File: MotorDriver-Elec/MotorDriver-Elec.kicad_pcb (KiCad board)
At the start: 2 copper layers, 129 x 149 mm, 9 parts, among them J4 Vmot, U1 Pico

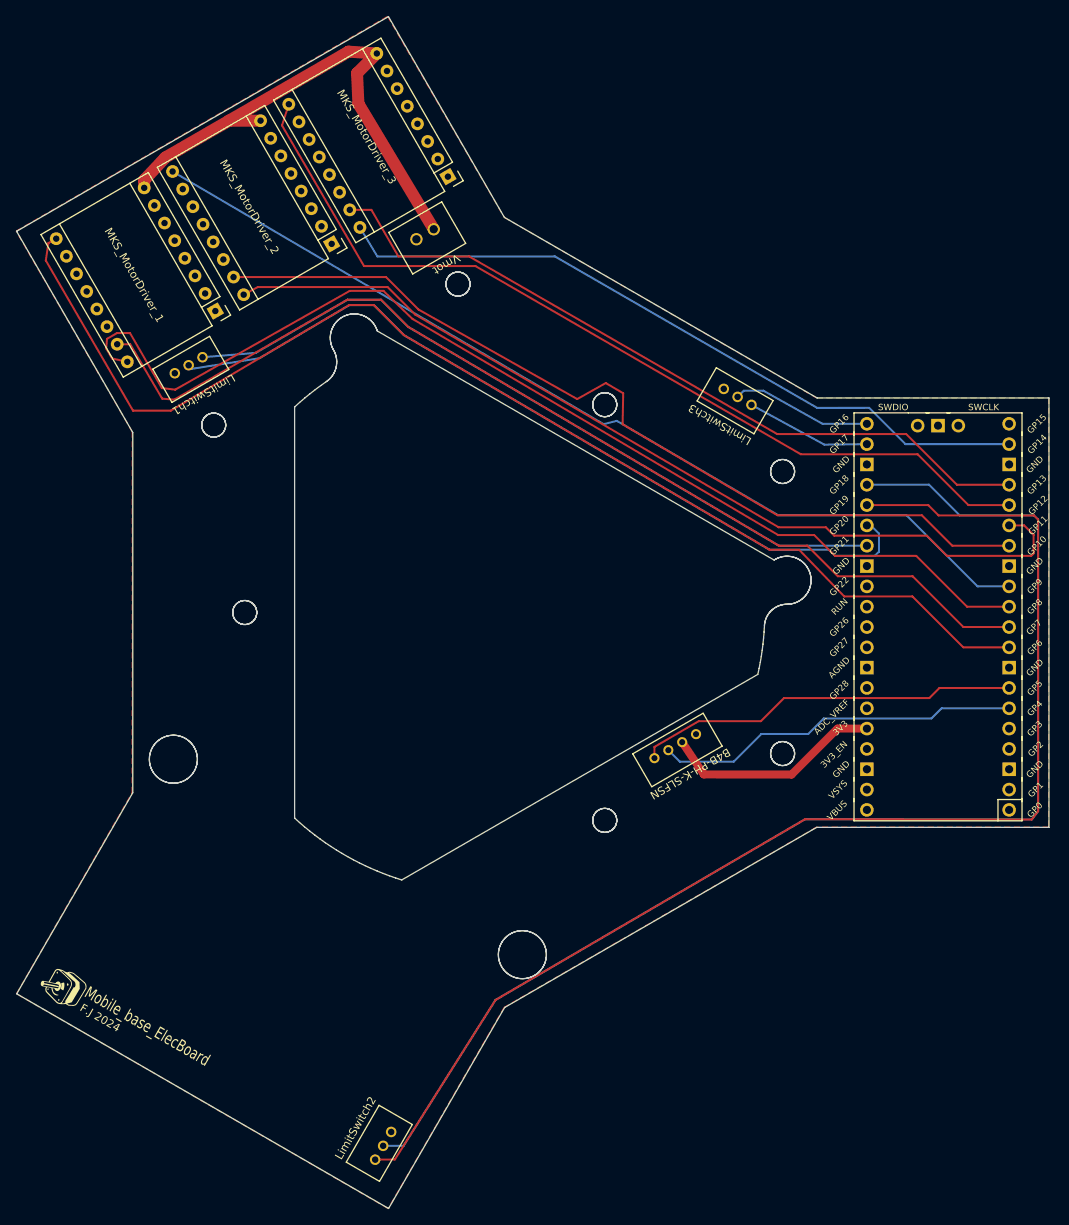
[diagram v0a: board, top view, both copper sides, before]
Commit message: Feat: add LED indicators
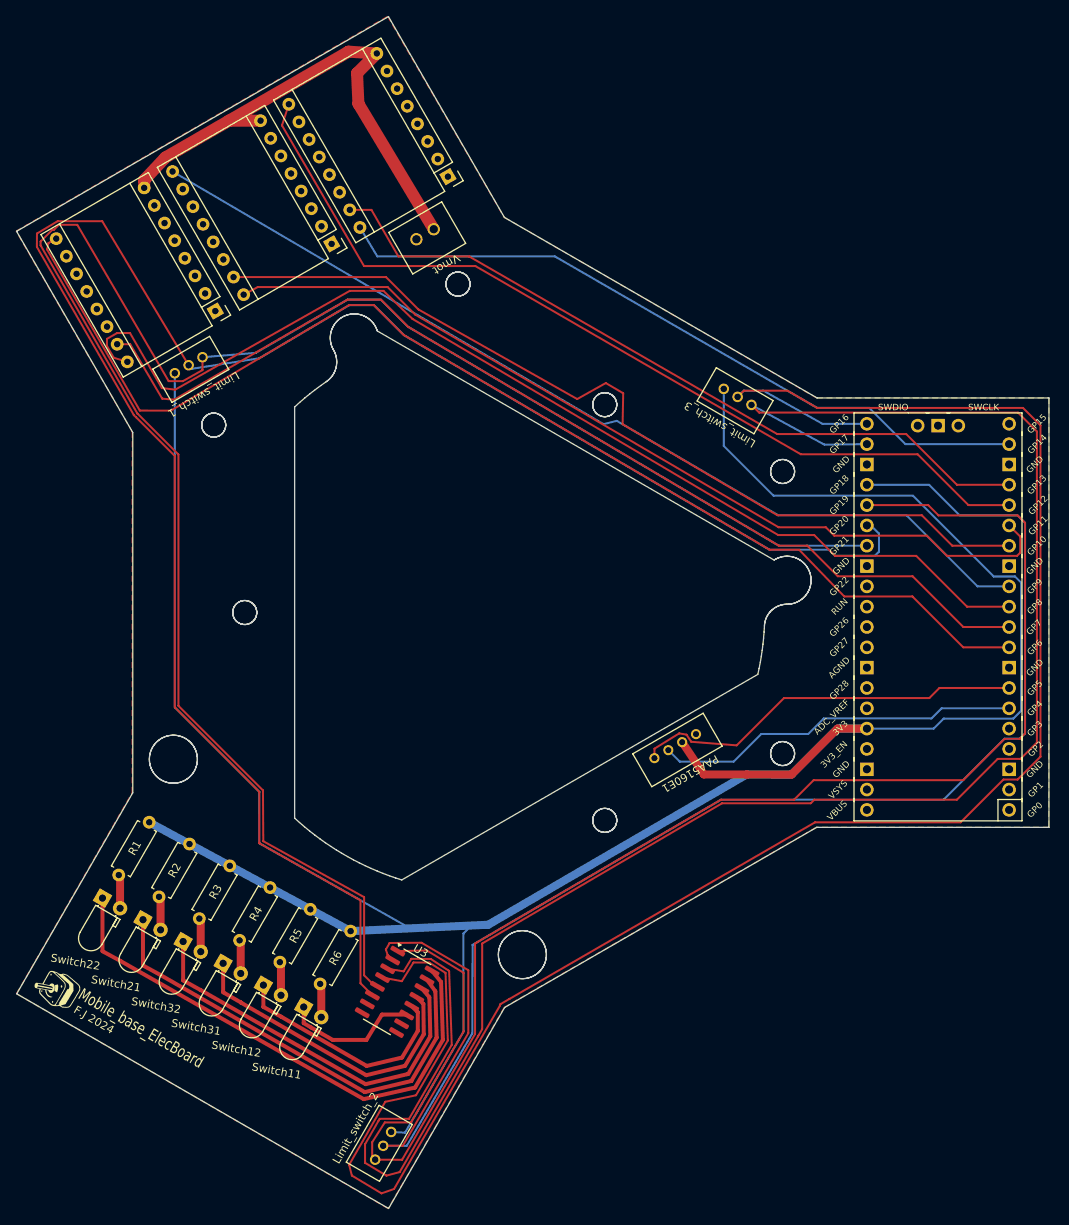
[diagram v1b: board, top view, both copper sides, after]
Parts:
- removed MKS_MotorDriver_1, MKS_MotorDriver_2, MKS_MotorDriver_3: Pololu_Breakout_A4988, Module:Pololu_Breakout-16_15.2x20.3mm
- added A1: MKS_MotorDriver_1, Module:Pololu_Breakout-16_15.2x20.3mm, F.Cu at (46.8, 57.5)
- added A2: MKS_MotorDriver_2, Module:Pololu_Breakout-16_15.2x20.3mm, F.Cu at (61.3, 49.1)
- added A3: MKS_MotorDriver_3, Module:Pololu_Breakout-16_15.2x20.3mm, F.Cu at (75.8, 40.7)
- added R1: 510, Resistor_THT:R_Axial_DIN0207_L6.3mm_D2.5mm_P7.62mm_Horizontal, F.Cu at (38.5, 121.4)
- added R2: 510, Resistor_THT:R_Axial_DIN0207_L6.3mm_D2.5mm_P7.62mm_Horizontal, F.Cu at (43.5, 124.1)
- added R3: 510, Resistor_THT:R_Axial_DIN0207_L6.3mm_D2.5mm_P7.62mm_Horizontal, F.Cu at (48.6, 126.9)
- added R4: 510, Resistor_THT:R_Axial_DIN0207_L6.3mm_D2.5mm_P7.62mm_Horizontal, F.Cu at (53.6, 129.6)
- added R5: 510, Resistor_THT:R_Axial_DIN0207_L6.3mm_D2.5mm_P7.62mm_Horizontal, F.Cu at (58.6, 132.3)
- added R6: 510, Resistor_THT:R_Axial_DIN0207_L6.3mm_D2.5mm_P7.62mm_Horizontal, F.Cu at (63.7, 135.0)
- added Switch11: Switch11, LED_THT:LED_D3.0mm_Horizontal_O1.27mm_Z2.0mm, F.Cu at (57.8, 144.5)
- added Switch12: Switch12, LED_THT:LED_D3.0mm_Horizontal_O1.27mm_Z2.0mm, F.Cu at (52.8, 141.8)
- added Switch21: Switch21, LED_THT:LED_D3.0mm_Horizontal_O1.27mm_Z2.0mm, F.Cu at (37.7, 133.6)
- added Switch22: Switch22, LED_THT:LED_D3.0mm_Horizontal_O1.27mm_Z2.0mm, F.Cu at (32.7, 130.9)
- added Switch31: Switch31, LED_THT:LED_D3.0mm_Horizontal_O1.27mm_Z2.0mm, F.Cu at (47.7, 139.0)
- added Switch32: Switch32, LED_THT:LED_D3.0mm_Horizontal_O1.27mm_Z2.0mm, F.Cu at (42.7, 136.3)
- added U3: ULN2003LV, Package_SO:SOIC-16_3.9x9.9mm_P1.27mm, F.Cu at (69.5, 142.6)
- Limit_switch_1: value LimitSwitch1 -> Limit_switch_1
- Limit_switch_2: value LimitSwitch2 -> Limit_switch_2
- Limit_switch_3: value LimitSwitch3 -> Limit_switch_3
- PAA5160E1: value B4B-PH-K-SLFSN -> PAA5160E1
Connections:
- Limit_switch_1 pad 1: GND -> 3.3V
- Limit_switch_2 pad 1: GND -> 3.3V
- Limit_switch_3 pad 1: GND -> 3.3V
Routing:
- net 3.3V: track 27.6 -> 332.7 mm
- net Int31: track 17.6 -> 248.7 mm
- net Int32: track 15.7 -> 243.7 mm
- net Int12: track 93.7 -> 239.1 mm
- net Int11: track 102.0 -> 244.5 mm
- net Net-(Switch22-K): track 0.00 -> 66.7 mm
- net Net-(Switch21-K): track 0.00 -> 57.5 mm
- net Net-(Switch32-K): track 0.00 -> 48.3 mm
- net Net-(Switch31-K): track 0.00 -> 38.8 mm
- net Int21: track 158.2 -> 195.7 mm
- net Int22: track 159.1 -> 194.9 mm
- net Net-(Switch12-K): track 0.00 -> 29.4 mm
- net Net-(Switch11-K): track 0.00 -> 17.2 mm
- net Net-(Switch22-A): track 0.00 -> 4.22 mm
- net Net-(Switch11-A): track 0.00 -> 4.22 mm
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
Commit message: Feat: add a 7mm hole for the lidar
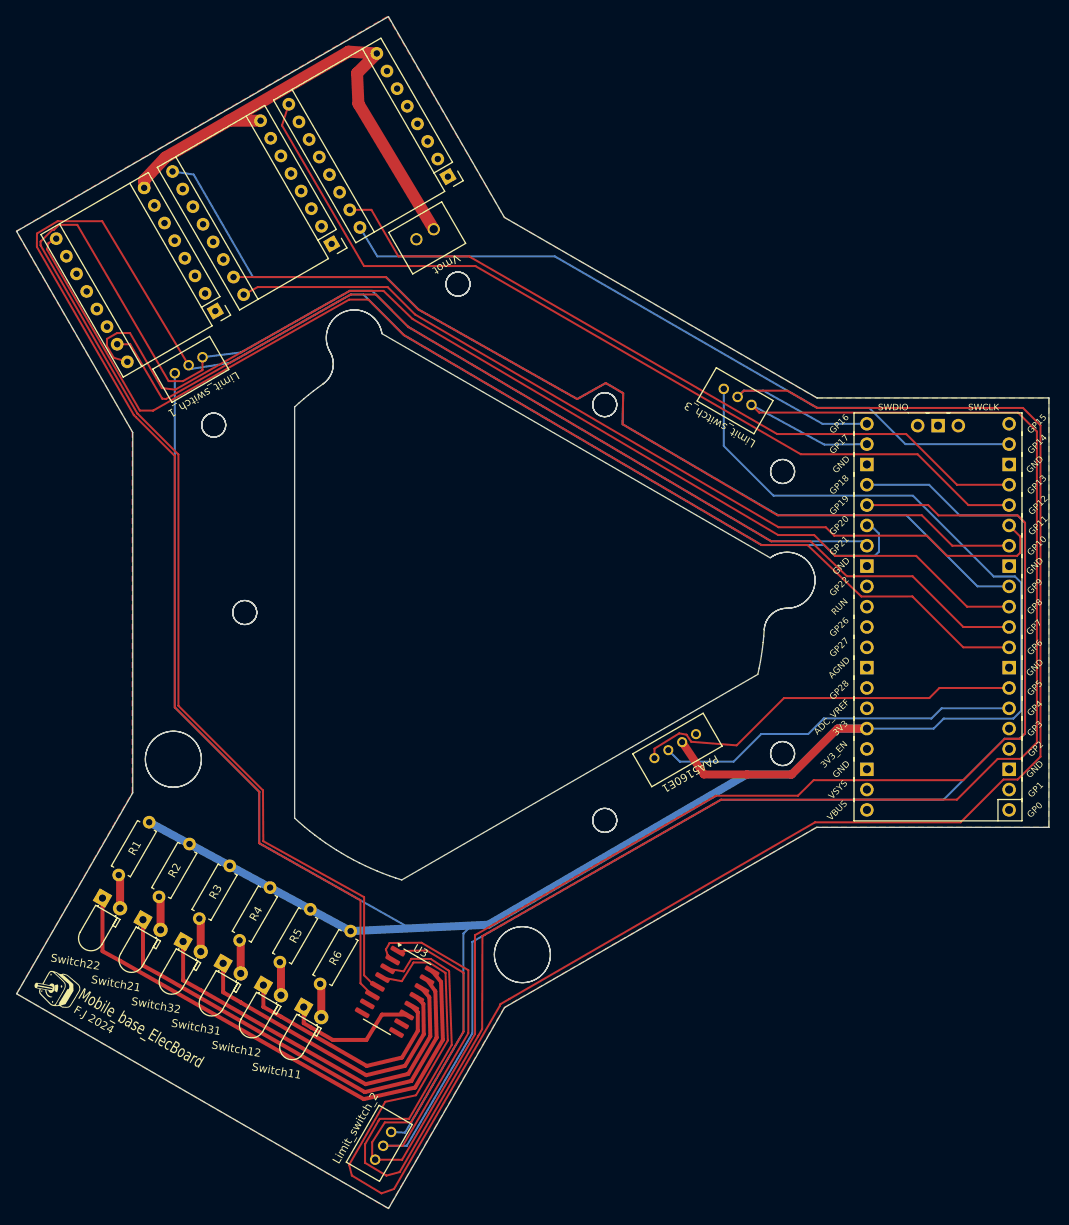
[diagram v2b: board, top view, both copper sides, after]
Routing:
- net En2: track 120.1 -> 128.2 mm
- net Int11: track 244.5 -> 245.5 mm
- net Int12: track 239.1 -> 239.9 mm
- net Int22: track 194.9 -> 195.6 mm
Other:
- outline, holes or cut-outs redrawn

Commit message: Fix: cutted ground plan and refactor LEDs position
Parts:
- moved Switch22 22.9 mm to (52.8, 141.8)
- moved R1 22.9 mm to (58.6, 132.3)
- moved R2 22.9 mm to (63.7, 135.0)
- moved Switch21 22.9 mm to (57.9, 144.5)
- moved Switch11 22.9 mm to (37.7, 133.6)
- moved R6 22.9 mm to (43.5, 124.1)
- moved R5 22.9 mm to (38.5, 121.4)
- moved Switch12 22.9 mm to (32.6, 130.9)
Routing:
- net 3.3V: track 332.7 -> 376.3 mm
- net Net-(Switch11-K): track 17.2 -> 47.3 mm
- net Net-(Switch21-K): track 57.5 -> 82.5 mm
- net Net-(Switch12-K): track 29.4 -> 52.7 mm
- net Net-(Switch22-K): track 66.7 -> 80.3 mm
- net Int31: track 248.7 -> 256.5 mm
- net STEP3: track 94.3 -> 96.1 mm
- net Int32: track 244.1 -> 245.6 mm
- net Int21: track 195.9 -> 194.7 mm

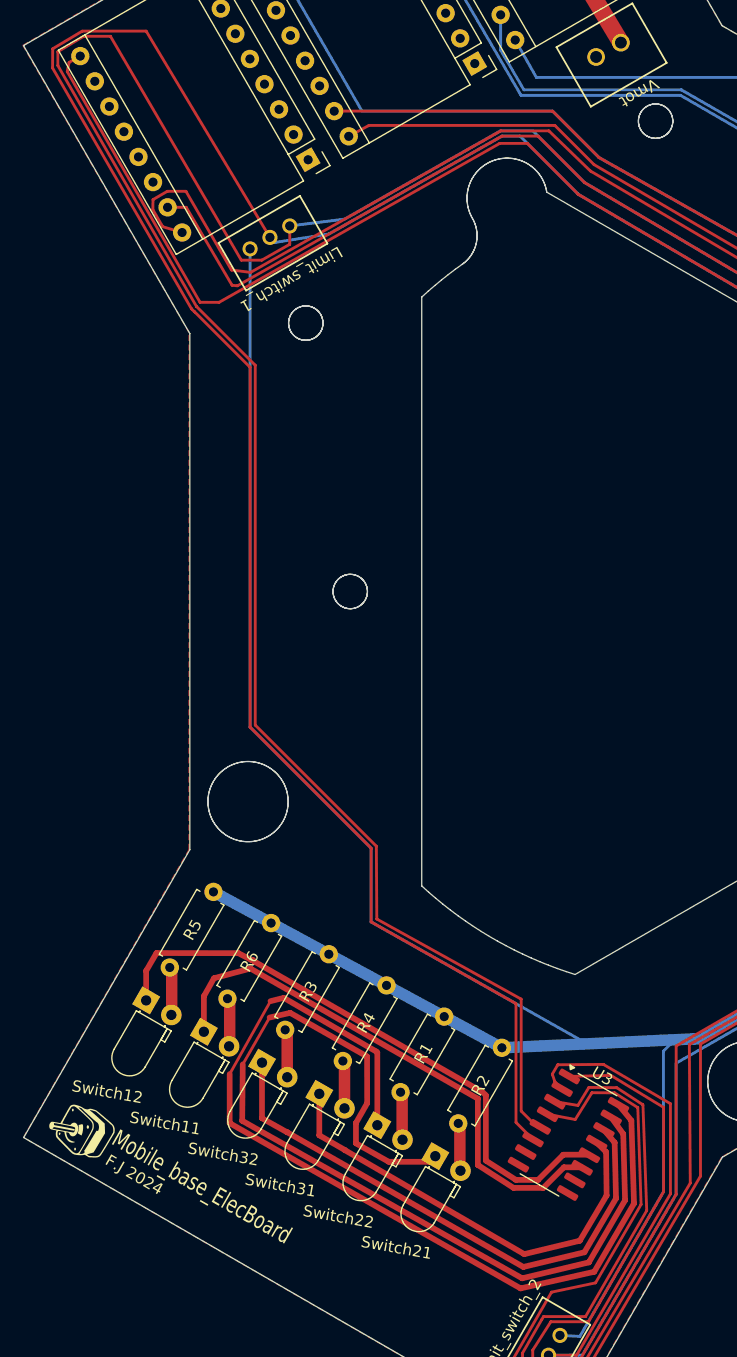
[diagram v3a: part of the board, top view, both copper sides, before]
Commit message: Fix: space between LEDs
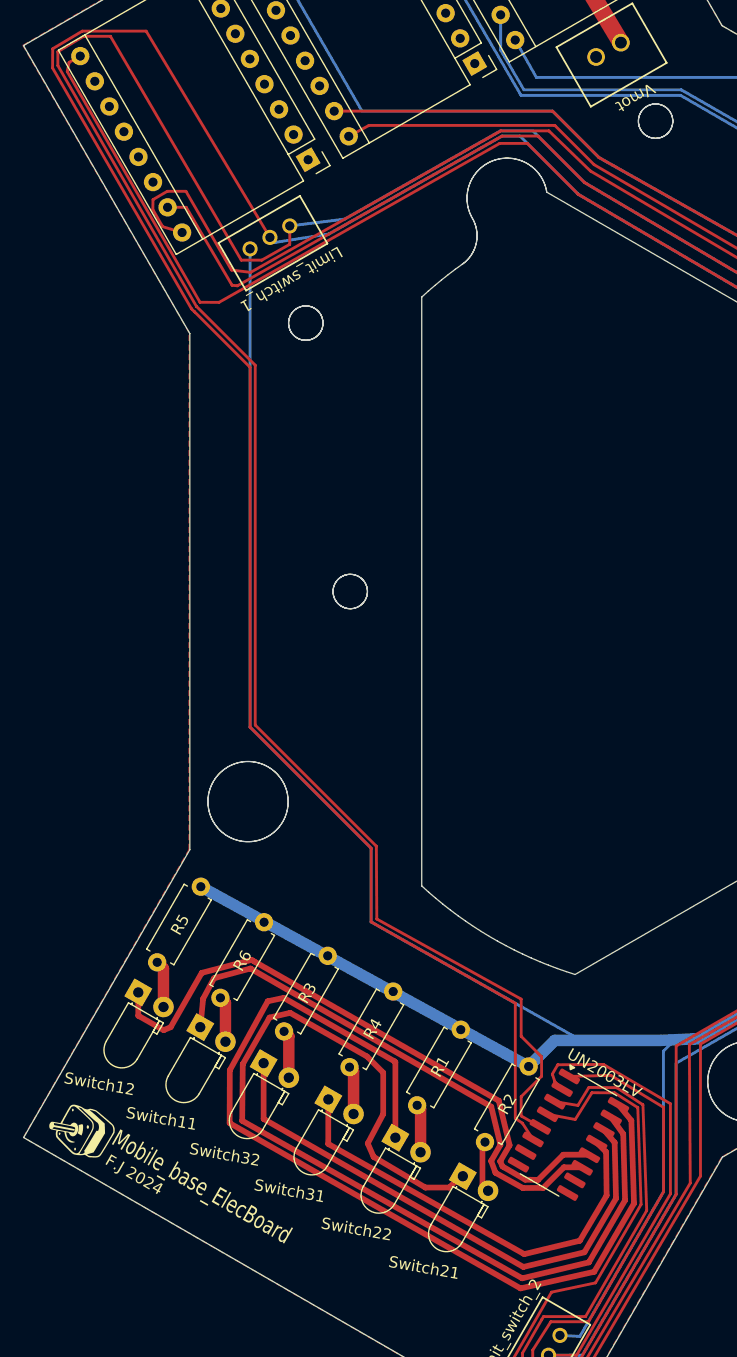
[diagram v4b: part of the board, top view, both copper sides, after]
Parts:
- removed J4: Vmot, CONN_B2B-XH-ALFSN_JST:CONN_B2B-XH-ALFSN_JST
- removed U3: ULN2003LV, Package_SO:SOIC-16_3.9x9.9mm_P1.27mm
- added UN2003LV1: UN2003LV, Package_SO:SOIC-16_3.9x9.9mm_P1.27mm, F.Cu at (69.5, 142.6)
- added Vmot1: Vmot, CONN_B2B-XH-ALFSN_JST:CONN_B2B-XH-ALFSN_JST, F.Cu at (71.9, 48.5)
- moved Switch21 2.98 mm to (60.3, 146.2)
- moved R2 2.85 mm to (66.0, 136.7)
- moved Switch22 1.92 mm to (54.4, 142.9)
- moved R1 1.84 mm to (60.1, 133.4)
- moved R5 1.19 mm to (37.4, 121.0)
- moved Switch12 0.98 mm to (31.9, 130.2)
- moved Switch31 0.93 mm to (48.5, 139.5)
- moved R4 0.79 mm to (54.2, 130.1)
- moved R6 0.62 mm to (42.9, 124.1)
- moved Switch11 0.51 mm to (37.3, 133.2)
- moved R3 0.17 mm to (48.5, 127.0)
- moved Switch32 0.15 mm to (42.9, 136.4)
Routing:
- net Net-(Switch21-K): track 82.5 -> 85.8 mm
- net 3.3V: track 376.3 -> 378.9 mm
- net Net-(Switch12-K): track 52.7 -> 55.0 mm
- net Net-(Switch22-K): track 80.3 -> 82.5 mm
- net Int12: track 240.2 -> 241.8 mm
- net Net-(Switch31-K): track 38.8 -> 38.0 mm
